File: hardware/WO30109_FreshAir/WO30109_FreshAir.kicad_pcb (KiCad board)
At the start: 2 copper layers, 63.4 x 107.2 mm, 76 parts, among them J5 DI 12V/IN1-4/COM/GND, K1 G5Q-1 DC12, K2 G5Q-1 DC12, K3 G5Q-1 DC12, K4 G5Q-1 DC12, P1 AC IN 230V, P2 PROG, P3 AC OUT, Q1 Si2302CDS, Q2 Si2302CDS, Q3 Si2302CDS, Q4 Si2302CDS, U1 ESP32-C6-WROOM-1-N8, U2 IRM-02-12, U3 SYN480R, U4 AP63203WU-7, U5 TLP290-4, U6 ST25DV04KC-IE6S3, Y1 13.52127MHz 20pF

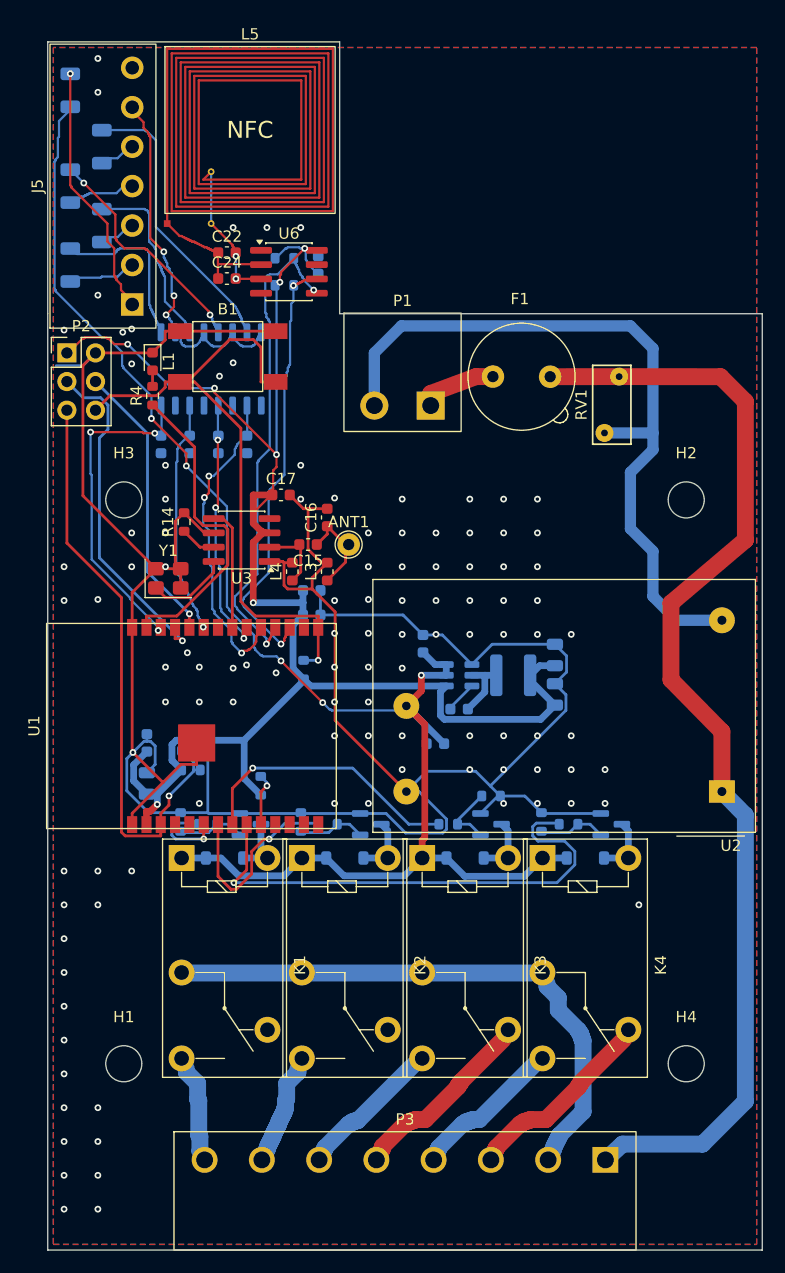
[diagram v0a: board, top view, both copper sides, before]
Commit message: hw: V3.4 照外殼 4-02-3 放回原板框（DI 2.54mm、NFC 外接 FPC 天線）
外殼是精鋼塑模 4-02-3（35mm 導軌盒 88×72×59，螺絲 50×50）；原板 63.4×83.08 本來就是照它做的。
V3.2／V3.3 加高的板子放不進外殼，V3.3 的板上 NFC 線圈離前蓋 >50mm 讀不到。

- J5 改 KF2EDGR-2.54-7P（C577599），和 P1 共用上方開窗，焊盤離市電 9.08mm
- NFC 板上線圈拿掉，J6（JST SH 2P，C160388）接 FPC 天線；C22/C24 依天線電感調諧（不上件）
- P2 改背面 2×3 燒錄測試點；B1 改 TS-1088（C720477 基礎料）放 J5 後方
- build_v34.sh：從 V3.1 換件擺件，低壓全部 Freerouting 重佈（第一輪即 0 未連線）
- mains_router.board_height() 不再把板邊線寬算進去（格點偏 0.05mm）
- ERC 0；DRC 錯誤 0、未連線 0、parity 0；CPL J6 以 JLC 封裝改正為 180°

Co-Authored-By: Claude Opus 5.5 (1M context) <noreply@anthropic.com>
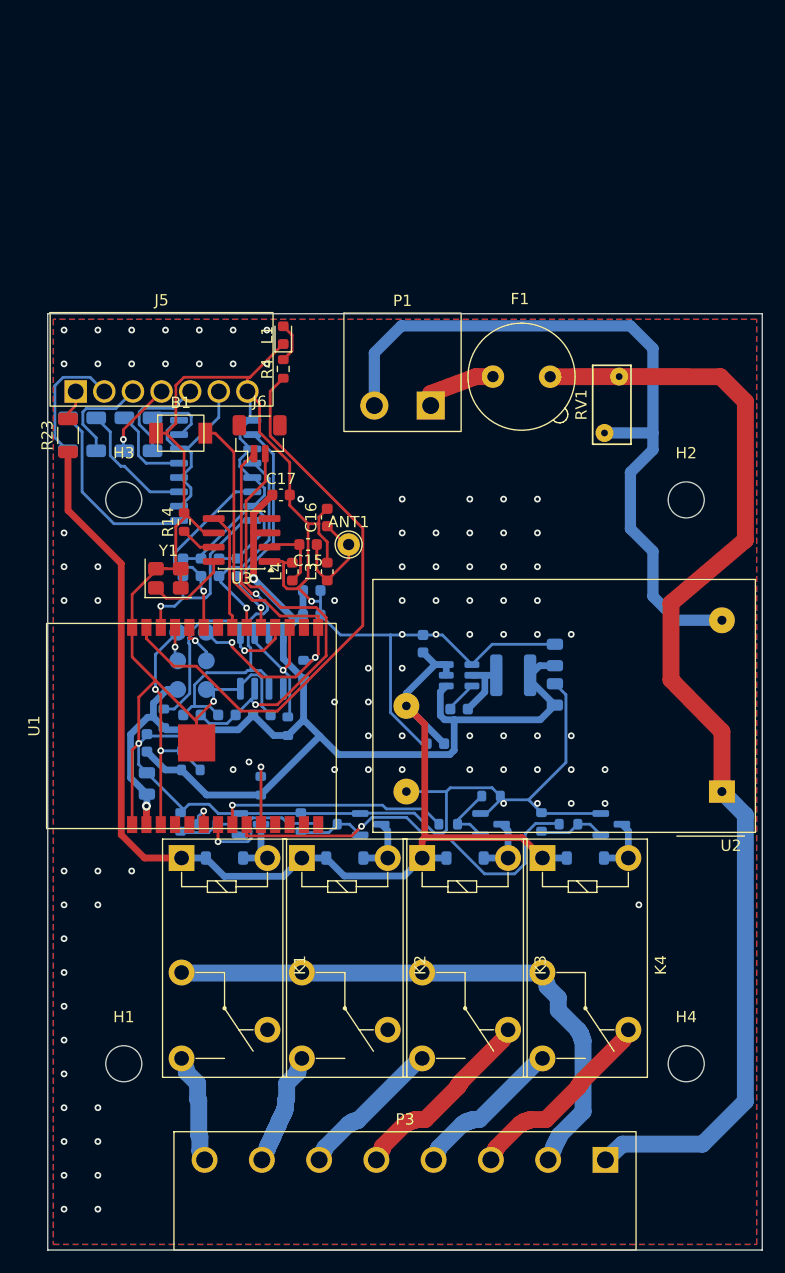
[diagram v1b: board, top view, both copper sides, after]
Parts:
- removed L5: NFC coil 1.27uH, WOOW:NFC_Coil_14.9x14.6mm_8T
- added J6: NFC ANT, Connector_JST:JST_SH_BM02B-SRSS-TB_1x02-1MP_P1.00mm_Vertical, F.Cu at (118.8, 111.1)
- B1: value ZX-QC66-4.3TP -> TS-1088-AR02016; footprint WOOW:SW_Push_6x6mm_SMD_ZX-QC66 -> WOOW:SW_SPST_TS-1088
- C22: value 75pF C0G -> DNP tune; moved to B.Cu
- C24, U6: moved to B.Cu
- J5: footprint WOOW:TerminalBlock_Pluggable_1x07_P3.50mm_Horizontal -> WOOW:TerminalBlock_Pluggable_1x07_P2.54mm_Horizontal
- P2: footprint Connector_PinHeader_2.54mm:PinHeader_2x03_P2.54mm_Vertical -> WOOW:ProgPads_2x03_P2.54mm; moved to B.Cu
- R23: moved to F.Cu
- moved R24 42.2 mm to (110.3, 135.9), turned to 90 degrees
- moved C22 41.0 mm to (115.9, 135.6)
- moved C23 40.2 mm to (119.0, 135.6), turned to 0 degrees
- moved R25 39.1 mm to (121.3, 136.6), turned to 90 degrees
- moved C24 38.8 mm to (112.8, 135.6)
- moved U6 34.6 mm to (119.0, 130.8), turned to 90 degrees
- moved R23 30.6 mm to (101.8, 110.8)
- moved P2 29.5 mm to (112.8, 130.8)
- moved R18 25.9 mm to (109.3, 110.7)
- moved R17 22.5 mm to (106.8, 110.7)
- moved R16 18.5 mm to (104.3, 110.7)
- moved J5 18.4 mm to (110.1, 106.9), turned to 0 degrees
- moved R15 15.0 mm to (101.8, 110.7)
- moved R4 11.8 mm to (120.9, 104.9)
- moved L1 11.8 mm to (120.9, 101.9), turned to 90 degrees
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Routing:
- net /+3V3: track 151.5 -> 115.1 mm, vias 7 -> 2
- net /EN: track 52.8 -> 22.3 mm, vias 1 -> 2
- net /+12V: track 138.3 -> 108.9 mm, vias 5 -> 0
- net /U0TXD: track 30.5 -> 3.07 mm
- net /NFC_AC1: track 12.6 -> 39.3 mm, vias 2 -> 1
- net /NFC_SCL: track 39.3 -> 12.8 mm, vias 2 -> 1
- net /NFC_SDA: track 44.1 -> 19.6 mm, vias 2 -> 1
- net /NFC_AC0: track 11.7 -> 36.0 mm, vias 0 -> 1
- net /LED: track 28.1 -> 51.8 mm
- net /U0RXD: track 25.3 -> 3.79 mm
- net /+12V_DI: track 22.8 -> 2.72 mm, vias 1 -> 0
- net /DI_A4: track 25.5 -> 5.86 mm
- net /DI_COM: track 34.1 -> 17.2 mm, vias 3 -> 0
- net /BOOT: track 56.7 -> 40.7 mm, vias 1 -> 2
- net /GND: track 245.5 -> 260.0 mm, vias 109 -> 92
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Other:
- board size 63.4 x 107.2 mm -> 63.4 x 83.1 mm
- board text removed: "12V"
- board text removed: "COM"
- board text removed: "GND"
- board text removed: "IN1"
- board text removed: "IN2"
- board text removed: "IN3"
- board text removed: "IN4"

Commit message: hw(v3.4): F1／P1／P3 改 JLC 代焊；修正端子 CPL 開口方向（J5 原本會朝板內）
使用者 10/07：「要 JLC 那邊都處理完」。
- P1 KEFA KF2EDGR-5.0-2P（C441193）、P3 KF2EDGR-5.08-8P（C441210）：腳距相符；
  規格書建議孔 Ø1.6，封裝與板上孔徑 1.5 → 1.6（焊盤大小不變，市電間距不受影響）
- F1 Littelfuse 37213150411 TR5 T3.15A（C178794）直接焊在 TR5 封裝（腳距 5.08、孔 Ø1.0 符合）；
  不用保險絲座（座子能代焊，但保險絲插進座子要人工）
- make_jlc_files：新增 solve_rotation_by_body()。插拔式端子焊盤一排等距，怎麼轉都對得上，
  依編號求角度會讓開口朝錯邊；改用板上 courtyard 與 JLC 絲印外框比本體方向。
  快取 jlc_footprints.json 多存 JLC 絲印外框（silk）
- 結果：J5 0°→180°（10/5 報價的 CPL 開口朝板內，未下單）、P1 180°、P3 0°（依編號會給 180°）

驗證：ERC 0；DRC 0 錯誤、0 未連線、0 原理圖不一致；test_make_jlc_files 11/11（新增 5 項）；
make_jlc_files --check exit 0；BOM 34 種／68 顆、手焊清單為空；
CPL 與 10/5 版差異只有 J5 角度與新增 F1／P1／P3。

Co-Authored-By: Claude Opus 5.5 (1M context) <noreply@anthropic.com>
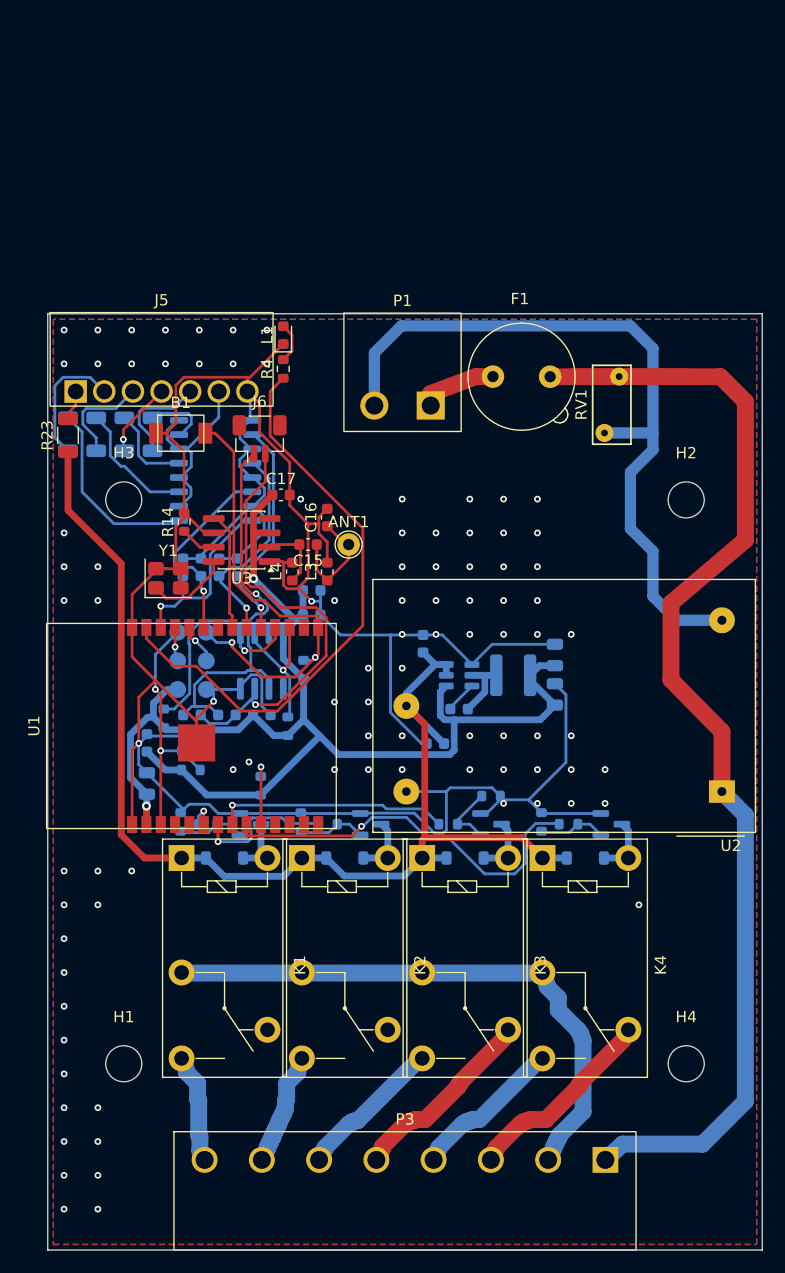
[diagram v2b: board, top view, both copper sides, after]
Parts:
- F1: value T3.15A 250V -> T3.15A 250V TR5
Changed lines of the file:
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@@
 			)
 		)
-		(property "Value" "T3.15A 250V"
+		(property "Value" "T3.15A 250V TR5"
 			(at 2.39 7.43 0)
 			(layer "F.Fab")
@@
 			)
 		)
-		(property "LCSC" ""
+		(property "LCSC" "C178794"
 			(at 0 0 0)
 			(layer "F.Fab")
@@
 			)
 		)
-		(property "LCSC" ""
+		(property "LCSC" "C441193"
 			(at 0 0 0)
 			(layer "F.Fab")
@@
 			(at 2.5 0)
 			(size 2.5 2.5)
-			(drill 1.5)
+			(drill 1.6)
 			(layers "*.Cu" "*.Mask")
 			(remove_unused_layers no)
@@
 			(at -2.5 0)
 			(size 2.5 2.5)
-			(drill 1.5)
+			(drill 1.6)
 			(layers "*.Cu" "*.Mask")
 			(remove_unused_layers no)
@@
 			)
 		)
-		(property "LCSC" ""
+		(property "LCSC" "C441210"
 			(at 0 0 0)
 			(layer "F.Fab")
@@
 			(at 17.78 0)
 			(size 2.3 2.3)
-			(drill 1.5)
+			(drill 1.6)
 			(layers "*.Cu" "*.Mask")
 			(remove_unused_layers no)
@@
 			(at 12.7 0)
 			(size 2.3 2.3)
-			(drill 1.5)
+			(drill 1.6)
 			(layers "*.Cu" "*.Mask")
 			(remove_unused_layers no)
@@
 			(at 7.62 0)
 			(size 2.3 2.3)
-			(drill 1.5)
+			(drill 1.6)
 			(layers "*.Cu" "*.Mask")
 			(remove_unused_layers no)
@@
 			(at 2.54 0)
 			(size 2.3 2.3)
-			(drill 1.5)
+			(drill 1.6)
 			(layers "*.Cu" "*.Mask")
 			(remove_unused_layers no)
@@
 			(at -2.54 0)
 			(size 2.3 2.3)
-			(drill 1.5)
+			(drill 1.6)
 			(layers "*.Cu" "*.Mask")
 			(remove_unused_layers no)
@@
 			(at -7.62 0)
 			(size 2.3 2.3)
-			(drill 1.5)
+			(drill 1.6)
 			(layers "*.Cu" "*.Mask")
 			(remove_unused_layers no)
@@
 			(at -12.7 0)
 			(size 2.3 2.3)
-			(drill 1.5)
+			(drill 1.6)
 			(layers "*.Cu" "*.Mask")
 			(remove_unused_layers no)
@@
 			(at -17.78 0)
 			(size 2.3 2.3)
-			(drill 1.5)
-			(layers "*.Cu" "*.Mask")
-			(remove_unused_layers no)
+			(drill 1.6)
+			(layers "*.Cu" "*.Mask")
+			(remove_unused_layers no)

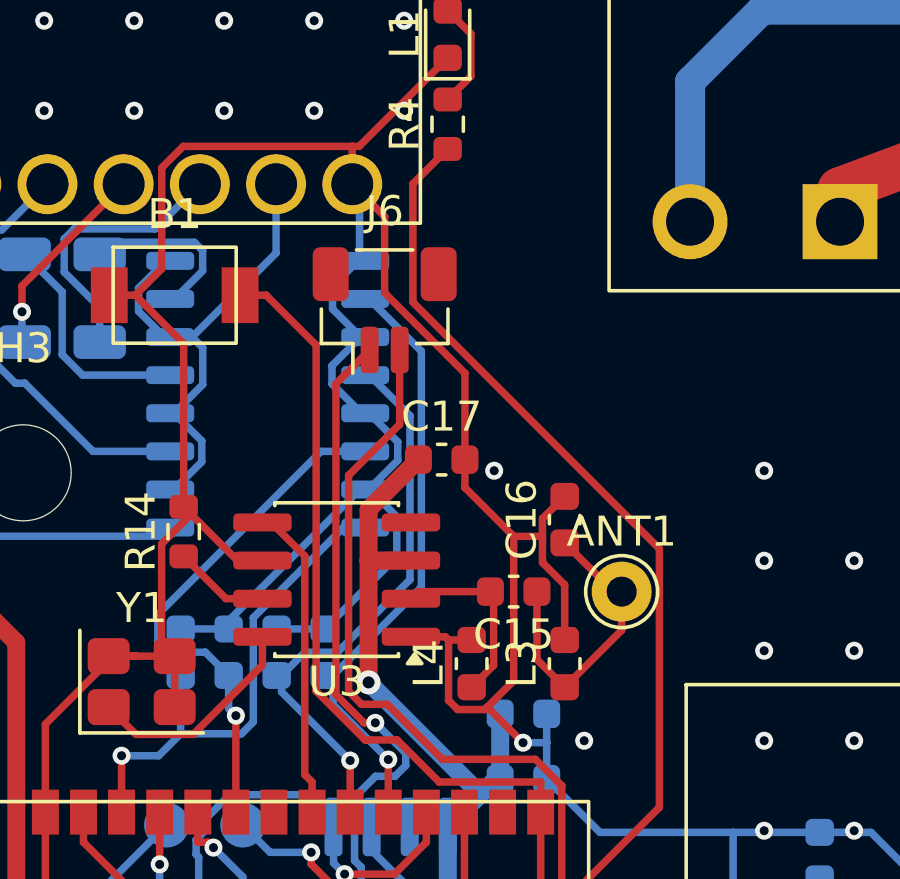
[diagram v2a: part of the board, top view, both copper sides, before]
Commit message: hw(v3.4): NFC 天線改插拔（Molex 1462362102＋J6 Micro-Lock Plus 座），C22 上 8.2pF
使用者 10/07：天線「用壓的不要用焊的」、選穩定的。
- 天線 Molex 1462362102：15×25mm、含 ferrite、102mm 雙絞線，線端 505565-0201＋505431-1000（霧錫）；
  DigiKey 庫存 2633、LCSC C3285166（Molex 1462360001-PS／產品頁確認）
- J6：JST SH → Molex 5055680271 直立 SMD（C5350147，鍍錫鉍，和端子同為錫）。新封裝
  WOOW:Molex_MicroLockPlus_505568-0271_1x02_P1.25mm_Vertical（焊盤取自 JLC 封裝）
- C22：La 3.3µH、Ca 4.9pF（PS 表）＋ST25DV 28.5pF → 8.2pF C0G（C1685，諧振約 13.58MHz）；C24 留空微調
- J6 擺放：新座固定腳較寬，原位置固定腳離 P1 市電只有 5.78mm（規則 6.4）且和 J5 courtyard 重疊。
  網格搜尋後改放 (118.5, 112.0) 0°：固定腳 6.63mm；拆掉碰到的 12 段正面走線，
  NFC_AC0／AC1／LED／BOOT 依 DRC 未連線清單用 A* 補線（GND 由鋪銅接通）
- mains_router：沒有網路的銅（MP 固定腳）原本一律當市電（離它 6.5mm），把 J6 自己的訊號腳圍死；
  改交給 is_mains 判斷（繞市電時行為不變，繞低壓時用小間距）
- gen_schematic：C22 有料號時進 BOM
- jlc_footprints.json：C5350147 EasyEDA 抓不下來，焊盤取自同系列 C5356739（其封裝檔名即 5055680271）

驗證：ERC 0；DRC 0 錯誤、0 未連線、0 原理圖不一致（含市電 6.4mm 規則）；
test_make_jlc_files 11/11；make_jlc_files --check exit 0（J6 依 JLC 封裝 180°）；BOM 35 種／69 顆、手焊清單為空。

Co-Authored-By: Claude Opus 5.5 (1M context) <noreply@anthropic.com>
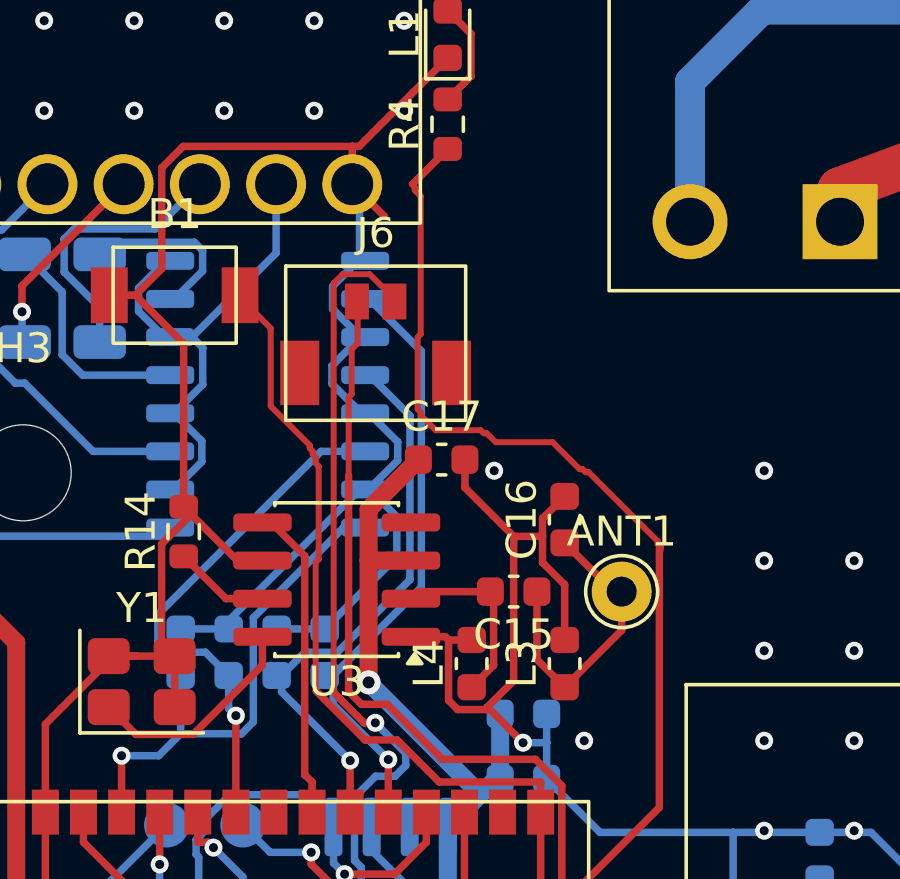
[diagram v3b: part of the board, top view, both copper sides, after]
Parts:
- C22: value DNP tune -> 8.2pF C0G
- J6: footprint Connector_JST:JST_SH_BM02B-SRSS-TB_1x02-1MP_P1.00mm_Vertical -> WOOW:Molex_MicroLockPlus_505568-0271_1x02_P1.25mm_Vertical
- moved J6 0.95 mm to (118.5, 112.0)
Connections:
- J6 pad 1: /NFC_AC0 -> /NFC_AC1
- J6 pad 2: /NFC_AC1 -> /NFC_AC0
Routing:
- net /GND: track 260.0 -> 250.7 mm
- net /NFC_AC0: track 36.0 -> 40.4 mm
- net /LED: track 51.8 -> 54.2 mm
- net /NFC_AC1: track 39.3 -> 40.4 mm
